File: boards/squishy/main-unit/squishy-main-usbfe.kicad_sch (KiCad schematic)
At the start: 42 parts, among them J1 USB_C_Receptacle, U1 LFE5UM5G-45F-8BG381C, U10 FUSB302BMPX, U13 HD3SS460, U14 TPD4E02B04DQA, U15 TPD4E02B04DQA, U17 USB3318, U4 SP3400-02UTG, X2 13MHz, X3 200MHz

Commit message: squishy: main: Some initial cleanup and assignment of part numbers and mfrs, still much to do,
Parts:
- C49, C50: MPN C0402C104M8PACTU -> C0603C104M5RACTU
- C51, C52, C81, C83: MFR (none) -> Murata Electronics; MPN (none) -> GRM155R71H104KE14D
- X2: footprint rhais_osc:SMD3225 -> rhais_osc:SMD2520; MFR (none) -> TXC CORPORATION; MPN (none) -> 8W-13.000MBE-T
- X3: footprint lethalbit:AK3A-xxxMHz -> lethalbit:AK2A-xxxMHz
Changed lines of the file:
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@@
 			)
 		)
-		(property "Datasheet" "~"
+		(property "Datasheet" "https://connect.kemet.com:7667/gateway/IntelliData-ComponentDocumentation/1.0/download/datasheet/C0402C103K3RACTU"
 			(at 243.84 99.06 0)
 			(effects
@@
 			)
 		)
-		(property "Datasheet" "~"
+		(property "Datasheet" "https://content.kemet.com/datasheets/KEM_C1006_X5R_SMD.pdf"
 			(at 320.04 31.75 0)
 			(effects
@@
 			)
 		)
-		(property "Datasheet" "~"
+		(property "Datasheet" "https://content.kemet.com/datasheets/KEM_C1006_X5R_SMD.pdf"
 			(at 242.57 36.83 0)
 			(effects
@@
 			)
 		)
-		(property "MPN" "C0402C104M8PACTU"
+		(property "MPN" "C0603C104M5RACTU"
 			(at 242.57 36.83 90)
 			(effects
@@
 			)
 		)
-		(property "Datasheet" "~"
+		(property "Datasheet" "https://content.kemet.com/datasheets/KEM_C1006_X5R_SMD.pdf"
 			(at 133.35 57.15 0)
 			(effects
@@
 			)
 		)
-		(property "Datasheet" "~"
+		(property "Datasheet" "https://content.kemet.com/datasheets/KEM_C1006_X5R_SMD.pdf"
 			(at 30.48 102.87 0)
 			(effects
@@
 			)
 		)
-		(property "Footprint" "lethalbit:AK3A-xxxMHz"
+		(property "Footprint" "lethalbit:AK2A-xxxMHz"
 			(at 83.82 271.78 0)
 			(effects
@@
 			)
 		)
-		(property "Datasheet" "~"
+		(property "Datasheet" "https://search.murata.co.jp/Ceramy/image/img/A01X/G101/ENG/GRM155R71H104KE14-01.pdf"
 			(at 111.76 34.29 0)
 			(effects
@@
 			)
 		)
-		(property "MFR" ""
+		(property "MFR" "Murata Electronics"
 			(at 111.76 34.29 90)
 			(effects
@@
 			)
 		)
-		(property "MPN" ""
+		(property "MPN" "GRM155R71H104KE14D"
 			(at 111.76 34.29 90)
 			(effects
@@
 			)
 		)
-		(property "Datasheet" "~"
+		(property "Datasheet" "https://content.kemet.com/datasheets/KEM_C1006_X5R_SMD.pdf"
 			(at 234.95 36.83 0)
 			(effects
@@
 			)
 		)
-		(property "MPN" "C0402C104M8PACTU"
+		(property "MPN" "C0603C104M5RACTU"
 			(at 234.95 36.83 90)
 			(effects
@@
 			)
 		)
-		(property "Footprint" "rhais_osc:SMD3225"
+		(property "Footprint" "rhais_osc:SMD2520"
 			(at 275.59 111.76 0)
 			(effects
@@
 			)
 		)
-		(property "Datasheet" ""
+		(property "Datasheet" "https://www.txccrystal.com/images/pdf/8w-tight.pdf"
 			(at 255.27 102.87 0)
 			(effects
@@
 			)
 		)
-		(property "MFR" ""
+		(property "MFR" "TXC CORPORATION"
 			(at 257.81 102.87 0)
 			(effects
@@
 			)
 		)
-		(property "MPN" ""
+		(property "MPN" "8W-13.000MBE-T"
 			(at 257.81 102.87 0)
 			(effects
@@
 			)
 		)
-		(property "Datasheet" "~"
+		(property "Datasheet" "https://connect.kemet.com:7667/gateway/IntelliData-ComponentDocumentation/1.0/download/specsheet/C0603C475K8PACTU"
 			(at 227.33 36.83 0)
 			(effects
@@
 			)
 		)
-		(property "Datasheet" "~"
+		(property "Datasheet" "https://search.murata.co.jp/Ceramy/image/img/A01X/G101/ENG/GRM155R71H104KE14-01.pdf"
 			(at 106.68 34.29 0)
 			(effects
@@
 			)
 		)
-		(property "MFR" ""
+		(property "MFR" "Murata Electronics"
 			(at 106.68 34.29 90)
 			(effects
@@
 			)
 		)
-		(property "MPN" ""
+		(property "MPN" "GRM155R71H104KE14D"
 			(at 106.68 34.29 90)
 			(effects
@@
 			)
 		)
-		(property "Datasheet" "~"
+		(property "Datasheet" "https://connect.kemet.com:7667/gateway/IntelliData-ComponentDocumentation/1.0/download/datasheet/C0402C103K3RACTU"
 			(at 115.57 262.89 0)
 			(effects
@@
 			)
 		)
-		(property "Datasheet" "~"
+		(property "Datasheet" "https://search.murata.co.jp/Ceramy/image/img/A01X/G101/ENG/GRM155R71H104KE14-01.pdf"
 			(at 124.46 240.03 0)
 			(effects
@@
 			)
 		)
+		(property "MFR" "Murata Electronics"
+			(at 124.46 240.03 0)
+			(effects
+				(font
+					(size 1.27 1.27)
+				)
+				(hide yes)
+			)
+		)
+		(property "MPN" "GRM155R71H104KE14D"
+			(at 124.46 240.03 0)
+			(effects
+				(font
+					(size 1.27 1.27)
+				)
+				(hide yes)
+			)
+		)
 		(pin "1"
 		)
@@
 			)
 		)
-		(property "Datasheet" "~"
+		(property "Datasheet" "https://search.murata.co.jp/Ceramy/image/img/A01X/G101/ENG/GRM155R71H104KE14-01.pdf"
 			(at 114.3 240.03 0)
 			(effects
@@
 			)
 		)
+		(property "MFR" "Murata Electronics"
+			(at 114.3 240.03 0)
+			(effects
+				(font
+					(size 1.27 1.27)
+				)
+				(hide yes)
+			)
+		)
+		(property "MPN" "GRM155R71H104KE14D"
+			(at 114.3 240.03 0)
+			(effects
+				(font
+					(size 1.27 1.27)
+				)
+				(hide yes)
+			)
+		)
 		(pin "1"
 		)
@@
 			)
 		)
-		(property "Datasheet" "~"
+		(property "Datasheet" "https://www.yuden.co.jp/productdata/catalog/mlcc06_e.pdf"
 			(at 312.42 31.75 0)
 			(effects

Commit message: squishy: main: Some more sorting part numbers and just making sure things are kosher prior to a full proper schematic review
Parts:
- G6: value ~ -> Pride Flag; MFR (none) -> Trans
- G7: value ~ -> Pride Flag; MFR (none) -> Lesbian
- R12: MFR (none) -> Vishay Dale; MPN (none) -> CRCW04020000Z0ED
- R49: MFR (none) -> Bourns Inc.; MPN (none) -> CAY16-4701F4LF
- R5: footprint rhais_rcl:R0603 -> rhais_rcl:R0402; MFR (none) -> Vishay Dale; MPN (none) -> CRCW0402100RFKED
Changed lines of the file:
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@@
 			)
 		)
-		(property "Datasheet" ""
+		(property "Datasheet" "https://www.bourns.com/docs/Product-Datasheets/CATCAY.pdf"
 			(at 340.36 59.69 0)
 			(effects
@@
 					(size 1.524 1.524)
 				)
+				(hide yes)
 			)
 		)
@@
 			)
 		)
+		(property "MFR" "Bourns Inc."
+			(at 340.36 59.69 0)
+			(effects
+				(font
+					(size 1.27 1.27)
+				)
+				(hide yes)
+			)
+		)
+		(property "MPN" "CAY16-4701F4LF"
+			(at 340.36 59.69 0)
+			(effects
+				(font
+					(size 1.27 1.27)
+				)
+				(hide yes)
+			)
+		)
 		(pin "1"
 		)
@@
 			)
 		)
-		(property "Datasheet" ""
+		(property "Datasheet" "https://www.bourns.com/docs/Product-Datasheets/CATCAY.pdf"
 			(at 336.55 59.69 0)
 			(effects
@@
 					(size 1.524 1.524)
 				)
+				(hide yes)
 			)
 		)
@@
 			)
 		)
+		(property "MFR" "Bourns Inc."
+			(at 336.55 59.69 0)
+			(effects
+				(font
+					(size 1.27 1.27)
+				)
+				(hide yes)
+			)
+		)
+		(property "MPN" "CAY16-4701F4LF"
+			(at 336.55 59.69 0)
+			(effects
+				(font
+					(size 1.27 1.27)
+				)
+				(hide yes)
+			)
+		)
 		(pin "1"
 		)
@@
 			)
 		)
-		(property "Value" "~"
+		(property "Value" "Pride Flag"
 			(at 393.7 260.35 0)
 			(effects
@@
 			)
 		)
+		(property "MFR" "Lesbian"
+			(at 393.7 260.35 0)
+			(effects
+				(font
+					(size 1.27 1.27)
+				)
+				(hide yes)
+			)
+		)
 		(instances
 			(project "squishy-main"
@@
 			)
 		)
-		(property "Datasheet" "~"
+		(property "Datasheet" "https://www.vishay.com/docs/20035/dcrcwe3.pdf"
 			(at 228.6 55.88 0)
 			(effects
@@
 			)
 		)
-		(property "Datasheet" "~"
+		(property "Datasheet" "https://www.vishay.com/docs/28773/crcwce3.pdf"
 			(at 217.17 38.1 0)
 			(effects
@@
 			)
 		)
-		(property "Datasheet" ""
+		(property "Datasheet" "https://www.bourns.com/docs/Product-Datasheets/CATCAY.pdf"
 			(at 347.98 59.69 0)
 			(effects
@@
 					(size 1.524 1.524)
 				)
+				(hide yes)
 			)
 		)
@@
 			)
 		)
+		(property "MFR" "Bourns Inc."
+			(at 347.98 59.69 0)
+			(effects
+				(font
+					(size 1.27 1.27)
+				)
+				(hide yes)
+			)
+		)
+		(property "MPN" "CAY16-4701F4LF"
+			(at 347.98 59.69 0)
+			(effects
+				(font
+					(size 1.27 1.27)
+				)
+				(hide yes)
+			)
+		)
 		(pin "1"
 		)
@@
 			)
 		)
-		(property "Footprint" "rhais_rcl:R0603"
+		(property "Footprint" "rhais_rcl:R0402"
 			(at 88.9 262.89 0)
 			(effects
@@
 			)
 		)
-		(property "Datasheet" "~"
+		(property "Datasheet" "https://www.vishay.com/docs/20035/dcrcwe3.pdf"
 			(at 88.9 262.89 0)
 			(effects
@@
 			)
 		)
-		(property "MFR" ""
+		(property "MFR" "Vishay Dale"
 			(at 88.9 262.89 90)
 			(effects
@@
 			)
 		)
-		(property "MPN" ""
+		(property "MPN" "CRCW0402100RFKED"
 			(at 88.9 262.89 90)
 			(effects
@@
 			)
 		)
-		(property "Datasheet" "~"
+		(property "Datasheet" "https://www.vishay.com/docs/20035/dcrcwe3.pdf"
 			(at 270.51 102.87 0)
 			(effects
@@
 			)
 		)
-		(property "MFR" ""
+		(property "MFR" "Vishay Dale"
 			(at 270.51 102.87 90)
 			(effects
@@
 			)
 		)
-		(property "MPN" ""
+		(property "MPN" "CRCW04020000Z0ED"
 			(at 270.51 102.87 90)
 			(effects
@@
 			)
 		)
-		(property "Datasheet" "~"
+		(property "Datasheet" "https://www.vishay.com/docs/20035/dcrcwe3.pdf"
 			(at 30.48 97.79 0)
 			(effects
@@
 			)
 		)
-		(property "Value" "~"
+		(property "Value" "Pride Flag"
 			(at 367.03 260.35 0)
 			(effects
@@
 			)
 		)
+		(property "MFR" "Trans"
+			(at 367.03 260.35 0)
+			(effects
+				(font
+					(size 1.27 1.27)
+				)
+				(hide yes)
+			)
+		)
 		(instances
 			(project "squishy-main"
@@
 			)
 		)
-		(property "Datasheet" ""
+		(property "Datasheet" "https://www.bourns.com/docs/Product-Datasheets/CATCAY.pdf"
 			(at 344.17 59.69 0)
 			(effects
@@
 					(size 1.524 1.524)
 				)
+				(hide yes)
 			)
 		)
@@
 			(at 344.17 59.69 0)
 			(effects
+				(font
+					(size 1.27 1.27)
+				)
+				(hide yes)
+			)
+		)
+		(property "MFR" "Bourns Inc."
+			(at 344.17 59.69 0)
+			(effects
+				(font
+					(size 1.27 1.27)
+				)
+				(hide yes)
+			)
+		)
+		(property "MPN" "CAY16-4701F4LF"
+			(at 344.17 59.69 0)
+			(effects

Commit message: squishy: main: Some more part selection updates. Only a few left
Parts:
- C16: MFR (none) -> Murata Electronics; MPN (none) -> GRM188R61E106KA73D
- C49, C91: MFR (none) -> YAGEO; MPN (none) -> CC0603KRX7R9BB301
- C82, C84: MFR (none) -> Murata Electronics; MPN (none) -> GRM155R71C103KA01D
- C85: MFR (none) -> Murata Electronics; MPN (none) -> GCM155R71H102KA37D
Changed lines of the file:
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@@
 			)
 		)
-		(property "Datasheet" "~"
+		(property "Datasheet" "https://search.murata.co.jp/Ceramy/image/img/A01X/G101/ENG/GRM155R71C103KA01-01.pdf"
 			(at 119.38 240.03 0)
 			(effects
@@
 			)
 		)
+		(property "MFR" "Murata Electronics"
+			(at 119.38 240.03 0)
+			(effects
+				(font
+					(size 1.27 1.27)
+				)
+				(hide yes)
+			)
+		)
+		(property "MPN" "GRM155R71C103KA01D"
+			(at 119.38 240.03 0)
+			(effects
+				(font
+					(size 1.27 1.27)
+				)
+				(hide yes)
+			)
+		)
 		(pin "1"
 		)
@@
 			)
 		)
-		(property "Datasheet" "~"
+		(property "Datasheet" "https://www.yageo.com/upload/media/product/app/datasheet/mlcc/upy-gphc_x7r_6_3v-to-250v.pdf"
 			(at 294.64 69.85 0)
 			(effects
@@
 			)
 		)
-		(property "MFR" ""
+		(property "MFR" "YAGEO"
 			(at 294.64 69.85 90)
 			(effects
@@
 			)
 		)
-		(property "MPN" ""
+		(property "MPN" "CC0603KRX7R9BB301"
 			(at 294.64 69.85 90)
 			(effects
@@
 			)
 		)
-		(property "Datasheet" "~"
+		(property "Datasheet" "https://search.murata.co.jp/Ceramy/image/img/A01X/G101/ENG/GRM155R71C103KA01-01.pdf"
 			(at 129.54 240.03 0)
 			(effects
@@
 			)
 		)
+		(property "MFR" "Murata Electronics"
+			(at 129.54 240.03 0)
+			(effects
+				(font
+					(size 1.27 1.27)
+				)
+				(hide yes)
+			)
+		)
+		(property "MPN" "GRM155R71C103KA01D"
+			(at 129.54 240.03 0)
+			(effects
+				(font
+					(size 1.27 1.27)
+				)
+				(hide yes)
+			)
+		)
 		(pin "1"
 		)
@@
 			)
 		)
-		(property "Datasheet" "~"
+		(property "Datasheet" "https://search.murata.co.jp/Ceramy/image/img/A01X/G101/ENG/GCM155R71H102KA37-01.pdf"
 			(at 134.62 240.03 0)
 			(effects
@@
 			)
 		)
+		(property "MFR" "Murata Electronics"
+			(at 134.62 240.03 0)
+			(effects
+				(font
+					(size 1.27 1.27)
+				)
+				(hide yes)
+			)
+		)
+		(property "MPN" "GCM155R71H102KA37D"
+			(at 134.62 240.03 0)
+			(effects
+				(font
+					(size 1.27 1.27)
+				)
+				(hide yes)
+			)
+		)
 		(pin "1"
 		)
@@
 			)
 		)
-		(property "Datasheet" "~"
+		(property "Datasheet" "https://search.murata.co.jp/Ceramy/image/img/A01X/G101/ENG/GRM188R61E106KA73-01.pdf"
 			(at 299.72 31.75 0)
 			(effects
@@
 			)
 		)
-		(property "MFR" ""
+		(property "MFR" "Murata Electronics"
 			(at 299.72 31.75 90)
 			(effects
@@
 			)
 		)
-		(property "MPN" ""
+		(property "MPN" "GRM188R61E106KA73D"
 			(at 299.72 31.75 90)
 			(effects
@@
 			)
 		)
-		(property "Datasheet" "~"
+		(property "Datasheet" "https://www.yageo.com/upload/media/product/app/datasheet/mlcc/upy-gphc_x7r_6_3v-to-250v.pdf"
 			(at 302.26 69.85 0)
 			(effects
@@
 			)
 		)
-		(property "MFR" ""
+		(property "MFR" "YAGEO"
 			(at 302.26 69.85 90)
 			(effects
@@
 			)
 		)
-		(property "MPN" ""
+		(property "MPN" "CC0603KRX7R9BB301"
 			(at 302.26 69.85 90)
 			(effects

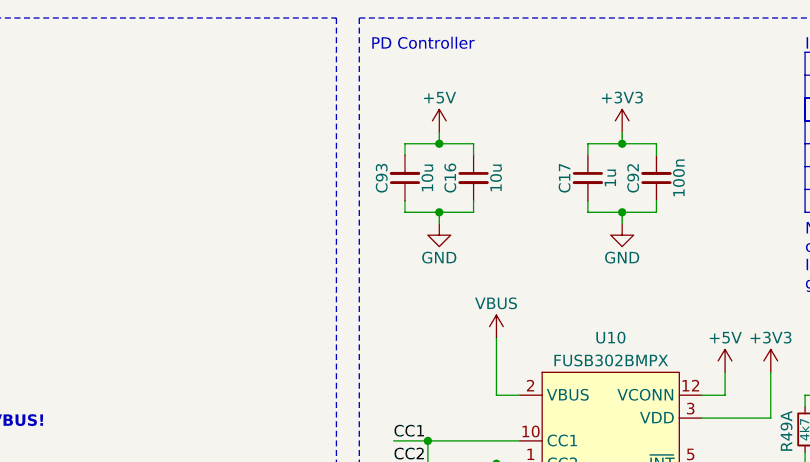
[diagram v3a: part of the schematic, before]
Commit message: squishy: main: got a big chunk of the USB front end done, and some other clean up with the PSU and the low voltage LDOs
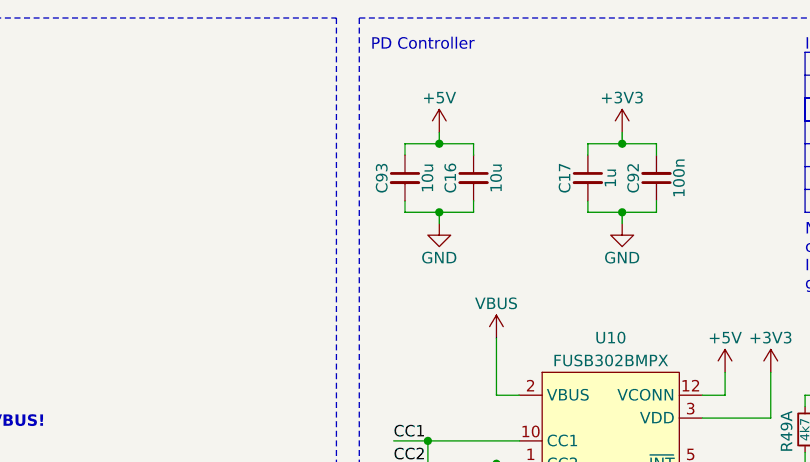
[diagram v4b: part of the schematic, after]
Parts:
- C93: footprint rhais_rcl:C0805 -> rhais_rcl:C0603; MPN GRM21BR61H106KE43L -> GRM188R61E106KA73D
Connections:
- net +5V: now also C93.1; no longer C93.2
- net GND: now also C93.2; no longer C93.1
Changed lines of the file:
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@@
+	(symbol
+		(lib_id "Device:C_Small")
+		(at 292.1 31.75 0)
+		(mirror y)
+		(unit 1)
+		(exclude_from_sim no)
+		(in_bom yes)
+		(on_board yes)
+		(dnp no)
+		(property "Reference" "C93"
+			(at 289.56 31.75 90)
+			(effects
+				(font
+					(size 1.27 1.27)
+				)
+			)
+		)
+		(property "Value" "10u"
+			(at 294.64 31.75 90)
+			(effects
+				(font
+					(size 1.27 1.27)
+				)
+			)
+		)
+		(property "Footprint" "rhais_rcl:C0603"
+			(at 292.1 31.75 0)
+			(effects
+				(font
+					(size 1.27 1.27)
+				)
+				(hide yes)
+			)
+		)
+		(property "Datasheet" "https://search.murata.co.jp/Ceramy/image/img/A01X/G101/ENG/GRM188R61E106KA73-01.pdf"
+			(at 292.1 31.75 0)
+			(effects
+				(font
+					(size 1.27 1.27)
+				)
+				(hide yes)
+			)
+		)
+		(property "Description" ""
+			(at 292.1 31.75 0)
+			(effects
+				(font
+					(size 1.27 1.27)
+				)
+				(hide yes)
+			)
+		)
+		(property "MFR" "Murata Electronics"
+			(at 292.1 31.75 90)
+			(effects
+				(font
+					(size 1.27 1.27)
+				)
+				(hide yes)
+			)
+		)
+		(property "MPN" "GRM188R61E106KA73D"
+			(at 292.1 31.75 90)
+			(effects
+				(font
+					(size 1.27 1.27)
+				)
+				(hide yes)
+			)
+		)
+		(pin "1"
+		)
+		(pin "2"
+		)
+		(instances
+			(project "squishy-main"
+				(path "/d4567381-92dd-4d3b-8c64-40007ced30aa/573264d1-b4a8-4279-b1ac-379f43fe1045"
+					(reference "C93")
+					(unit 1)
+				)
+			)
+		)
+	)
 	(symbol
 		(lib_id "Device:C_Small")
@@
 					(unit 1)
 				)
-			)
-		)
-	)
-	(symbol
-		(lib_id "Device:C_Small")
-		(at 292.1 31.75 180)
-		(unit 1)
-		(exclude_from_sim no)
-		(in_bom yes)
-		(on_board yes)
-		(dnp no)
-		(property "Reference" "C93"
-			(at 289.56 31.75 90)
-			(effects
-				(font
-					(size 1.27 1.27)
-				)
-			)
-		)
-		(property "Value" "10u"
-			(at 294.64 31.75 90)
-			(effects
-				(font
-					(size 1.27 1.27)
-				)
-			)
-		)
-		(property "Footprint" "rhais_rcl:C0805"
-			(at 292.1 31.75 0)
-			(effects
-				(font
-					(size 1.27 1.27)
-				)
-				(hide yes)
-			)
-		)
-		(property "Datasheet" "https://search.murata.co.jp/Ceramy/image/img/A01X/G101/ENG/GRM21BR61H106KE43-01A.pdf"
-			(at 292.1 31.75 0)
-			(effects
-				(font
-					(size 1.27 1.27)
-				)
-				(hide yes)
-			)
-		)
-		(property "Description" ""
-			(at 292.1 31.75 0)
-			(effects
-				(font
-					(size 1.27 1.27)
-				)
-				(hide yes)
-			)
-		)
-		(property "MFR" "Murata Electronics"
-			(at 292.1 31.75 90)
-			(effects
-				(font
-					(size 1.27 1.27)
-				)
-				(hide yes)
-			)
-		)
-		(property "MPN" "GRM21BR61H106KE43L"
-			(at 292.1 31.75 90)
-			(effects
-				(font
-					(size 1.27 1.27)
-				)
-				(hide yes)
-			)
-		)
-		(pin "1"
-		)
-		(pin "2"
-		)
-		(instances
-			(project "squishy-main"
-				(path "/d4567381-92dd-4d3b-8c64-40007ced30aa/573264d1-b4a8-4279-b1ac-379f43fe1045"
-					(reference "C93")
-					(unit 1)
-				)

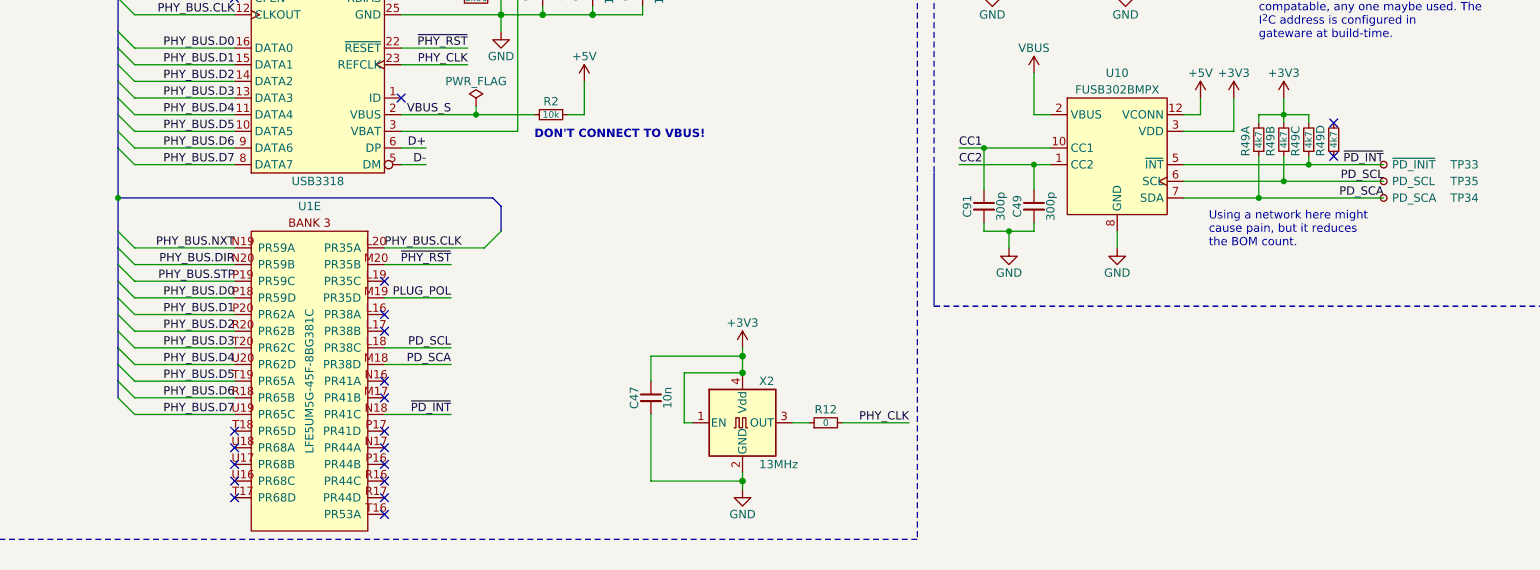
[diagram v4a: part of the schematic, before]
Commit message: squishy: main: A whole lot of work, changed the board footprint, wiggled the ULPI, and fixed up a fair whack of pads needing thermals
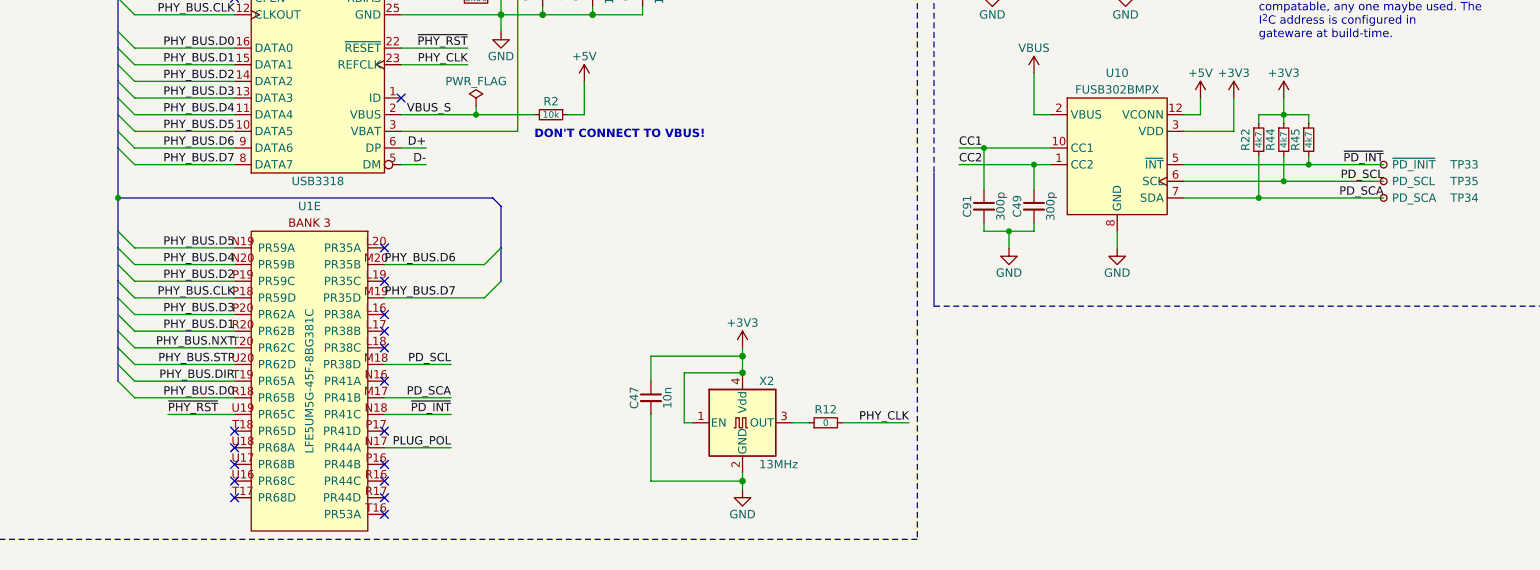
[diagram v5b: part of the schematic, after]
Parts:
- removed R49: 4k7, rhais_rcl:R0603_Array_Concave_4, symbol DX-MON:pkl_R4_Small
- added R22, R44, R45: 4k7, rhais_rcl:R0603, symbol Device:R_Small
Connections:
- net +3V3: now also R22.1, R44.1, R45.1
- net PD_SCA: now also U1.M17 (PR41B), R22.2; no longer U1.M18 (PR38D)
- net PD_SCL: now also U1.M18 (PR38D), R44.2; no longer U1.L18 (PR38C)
- net PHY_BUS.CLK: now also U1.P18 (PR59D); no longer U1.L20 (PR35A)
- net PHY_BUS.D0: now also U1.R18 (PR65B); no longer U1.P18 (PR59D)
- net PHY_BUS.D1: now also U1.R20 (PR62B); no longer U1.P20 (PR62A)
- net PHY_BUS.D2: now also U1.P19 (PR59C); no longer U1.R20 (PR62B)
- net PHY_BUS.D3: now also U1.P20 (PR62A); no longer U1.T20 (PR62C)
- net PHY_BUS.D4: now also U1.N20 (PR59B); no longer U1.U20 (PR62D)
- net PHY_BUS.D5: now also U1.N19 (PR59A); no longer U1.T19 (PR65A)
- net PHY_BUS.D6: now also U1.M20 (PR35B); no longer U1.R18 (PR65B)
- net PHY_BUS.D7: now also U1.M19 (PR35D); no longer U1.U19 (PR65C)
- net PHY_BUS.DIR: now also U1.T19 (PR65A); no longer U1.N20 (PR59B)
- net PHY_BUS.NXT: now also U1.T20 (PR62C); no longer U1.N19 (PR59A)
- net PHY_BUS.STP: now also U1.U20 (PR62D); no longer U1.P19 (PR59C)
- net PLUG_POL: now also U1.N17 (PR44A); no longer U1.M19 (PR35D)
- net ~{PD_INT}: now also R45.2
- net ~{PHY_RST}: now also U1.U19 (PR65C); no longer U1.M20 (PR35B)
- no-connect marks 54 -> 52
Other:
- note removed: "Using a network here might cause pain, but it reduces the BOM count."
